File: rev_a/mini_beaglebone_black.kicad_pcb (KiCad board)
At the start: 2 copper layers, 4 parts

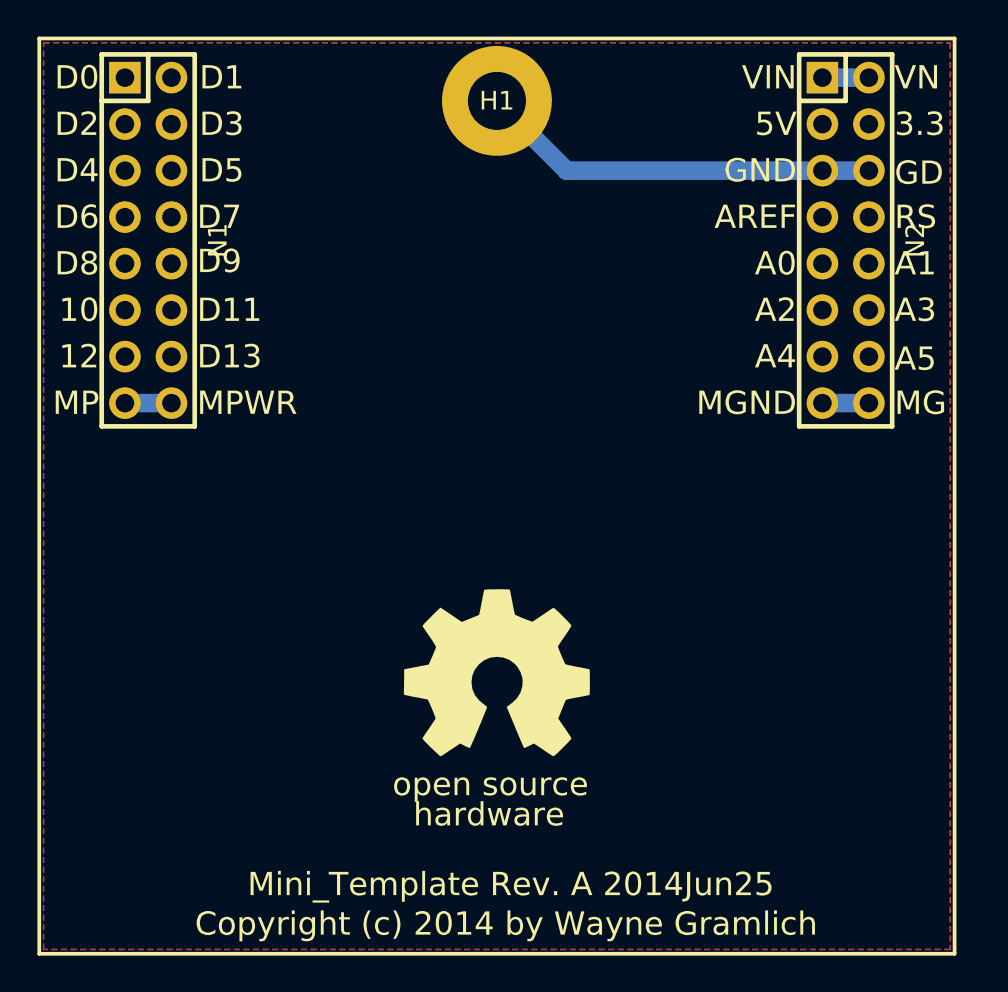
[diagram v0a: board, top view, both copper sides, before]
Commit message: Got first layout of BBB Mini-Shield done.
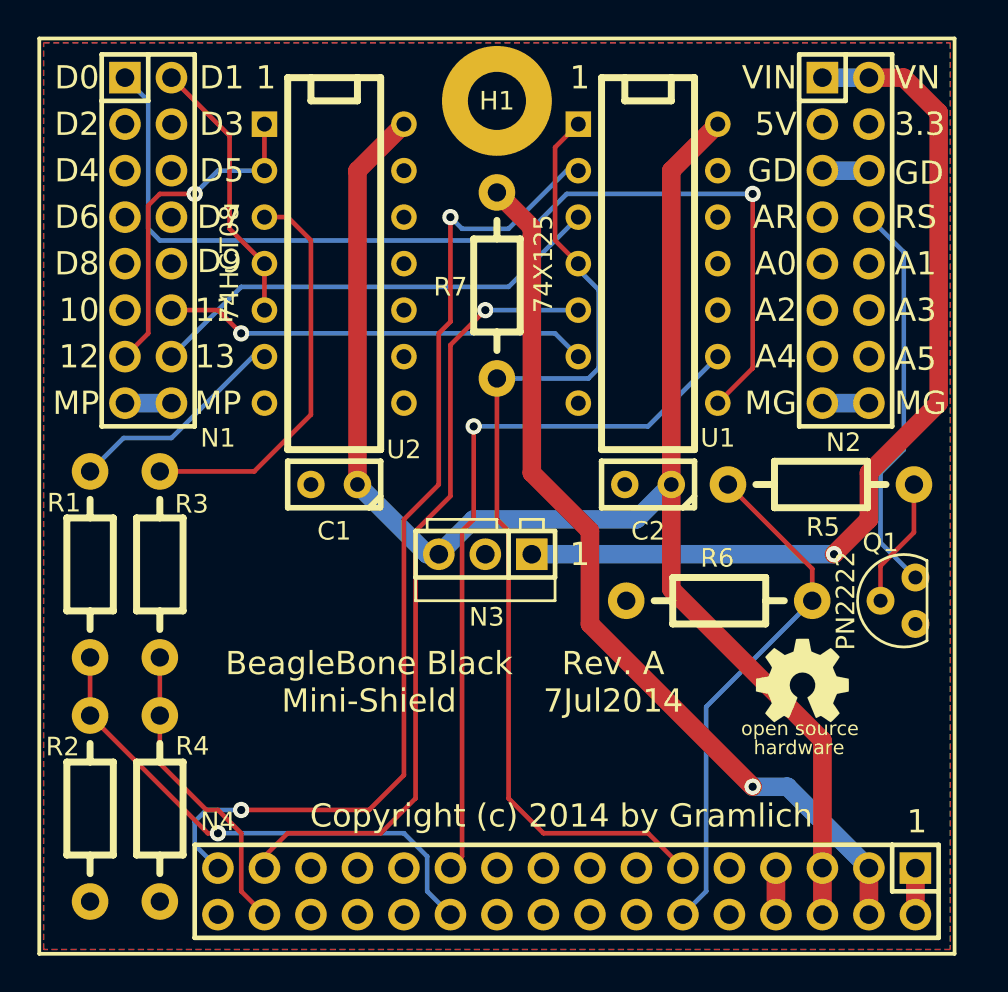
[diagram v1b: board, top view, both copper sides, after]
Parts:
- added C1: .1uF, Mini_BeagleBone_Black_Rev_A:Capacitor3MMDiscRM2.5, F.Cu at (92.7, 127.6)
- added C2: .1uF, Mini_BeagleBone_Black_Rev_A:Capacitor3MMDiscRM2.5, F.Cu at (109.9, 127.6)
- added N3: OKI-78SR-5/1.5-W36-C, Mini_BeagleBone_Black_Rev_A:OKI_DC_TO_DC_CONNECTOR, F.Cu at (101.0, 131.4)
- added N4: BBB_P9_HEADER, Mini_BeagleBone_Black_Rev_A:Pin_Header_Straight_2x16, F.Cu at (105.4, 149.9)
- added Q1: PN2222, Mini_BeagleBone_Black_Rev_A:TO92_123, F.Cu at (123.8, 134.0)
- added R1: 2K2 1%, Mini_BeagleBone_Black_Rev_A:Resistor_Horizontal_RM10mm, F.Cu at (79.4, 132.1)
- added R2: 3K3 1%, Mini_BeagleBone_Black_Rev_A:Resistor_Horizontal_RM10mm, F.Cu at (79.4, 145.4)
- added R3: 2K2 1%, Mini_BeagleBone_Black_Rev_A:Resistor_Horizontal_RM10mm, F.Cu at (83.2, 132.1)
- added R4: 3K3 1%, Mini_BeagleBone_Black_Rev_A:Resistor_Horizontal_RM10mm, F.Cu at (83.2, 145.4)
- added R5: 470, Mini_BeagleBone_Black_Rev_A:Resistor_Horizontal_RM10mm, F.Cu at (119.4, 127.6)
- added R6: 10K, Mini_BeagleBone_Black_Rev_A:Resistor_Horizontal_RM10mm, F.Cu at (113.7, 134.0)
- added R7: 10K, Mini_BeagleBone_Black_Rev_A:Resistor_Horizontal_RM10mm, F.Cu at (101.6, 116.8)
- added U1: 74X125, Mini_BeagleBone_Black_Rev_A:DIP-14__300, F.Cu at (109.9, 115.6)
- added U2: 74HCT08, Mini_BeagleBone_Black_Rev_A:DIP-14__300, F.Cu at (92.7, 115.6)
- G1: footprint Mini_BeagleBone_Black_Rev_A:OSHW_LOGO_400mil -> Mini_BeagleBone_Black_Rev_A:OSHW_LOGO_200mil
- moved G1 16.7 mm to (118.3, 138.3)
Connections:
- net /GND renamed GND
- N1 pad 1: (no net) -> /D0
- N1 pad 12: (no net) -> /D11
- N1 pad 13: (no net) -> /D12
- N1 pad 14: (no net) -> /D13
- N1 pad 2: (no net) -> /D1
- N2 pad 8: (no net) -> /~RESET
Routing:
- net VCC: track 0.00 -> 88.7 mm, vias 0 -> 1
- net Net-(N4-Pad11): track 0.00 -> 55.7 mm
- net Net-(N4-Pad31): track 0.00 -> 55.6 mm, vias 0 -> 2
- net /D0: track 0.00 -> 55.3 mm, vias 0 -> 1
- net /BB_VDD3V3: track 0.00 -> 49.1 mm, vias 0 -> 1
- net /VIN: track 2.54 -> 50.1 mm, vias 0 -> 1
- net Net-(N4-Pad29): track 0.00 -> 43.5 mm, vias 0 -> 1
- net Net-(N4-Pad21): track 0.00 -> 39.6 mm, vias 0 -> 1
- net Net-(N4-Pad22): track 0.00 -> 28.5 mm, vias 0 -> 1
- net Net-(N4-Pad12): track 0.00 -> 28.3 mm
- net /D13: track 0.00 -> 25.4 mm
- net /D11: track 0.00 -> 23.3 mm, vias 0 -> 1
- net /MISO_5V: track 0.00 -> 22.1 mm
- net /~RESET: track 0.00 -> 21.8 mm
- net /D12: track 0.00 -> 18.5 mm, vias 0 -> 1
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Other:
- board text added: "1"
- board text added: "11"
- board text added: "13"
- board text added: "AR"
- board text added: "BeagleBone Black Mini-Shield"
- board text added: "Copyright (c) 2014 by Gramlich"
- board text added: "Rev. A 6Jul2014"
- board text added: "Rev. A 7Jul2014"
- board text removed: "AREF"
- board text removed: "Copyright (c) 2014 by Wayne Gramlich"
- board text removed: "D11"
- board text removed: "D13"
- board text removed: "GND"
- board text removed: "MGND"
- board text removed: "MPWR"
- board text removed: "Mini_Template Rev. A 2014Jun25"

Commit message: Did another polishing sweep through the board.
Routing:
- net GND: track 5.08 -> 94.4 mm, vias 0 -> 4
- net /D0: track 55.3 -> 51.9 mm
- net /VIN: track 50.1 -> 48.7 mm
- net /D1: track 14.8 -> 15.9 mm
- net Net-(N4-Pad12): track 28.3 -> 28.6 mm, vias 0 -> 1
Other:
- board text added: "Rev. A 11Jul2014"
- board text added: "Rev. A1 11Jul2014"
- board text removed: "Rev. A 6Jul2014"
- board text removed: "Rev. A 7Jul2014"

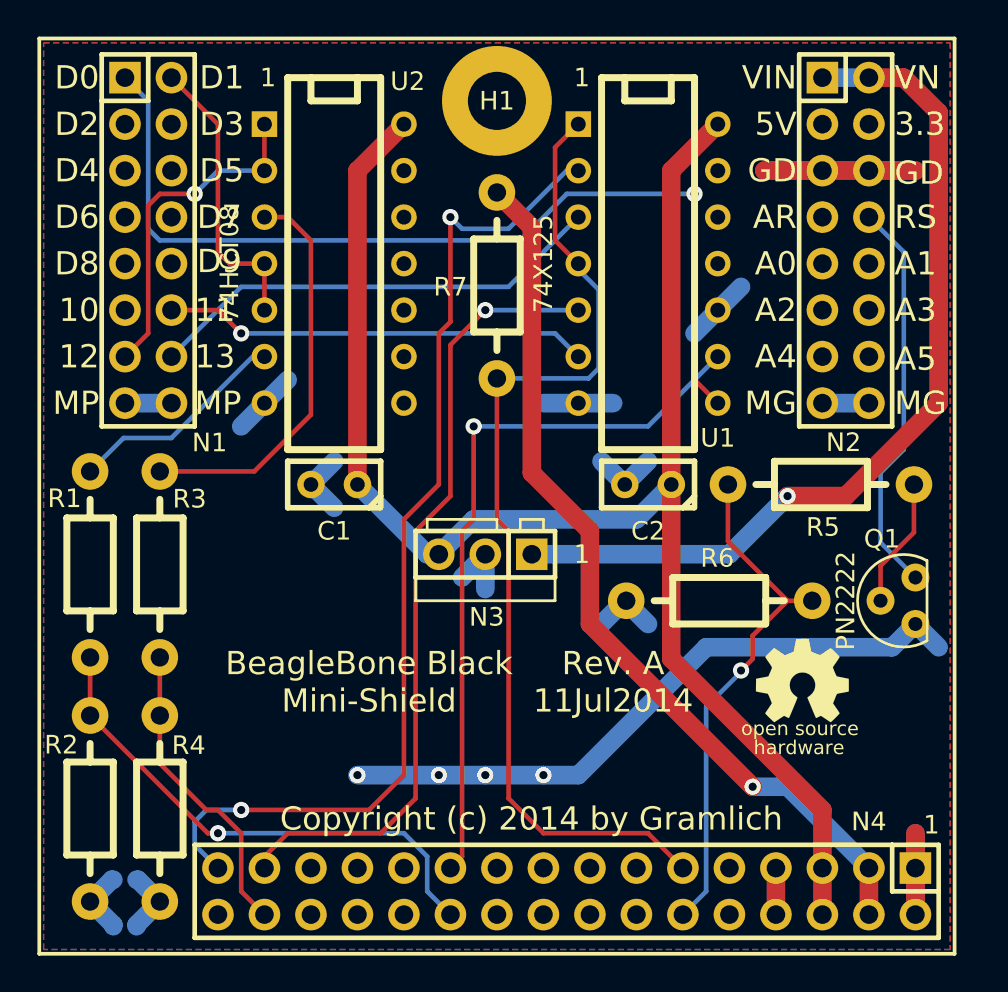
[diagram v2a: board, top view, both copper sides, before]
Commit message: Added Edge Cuts.
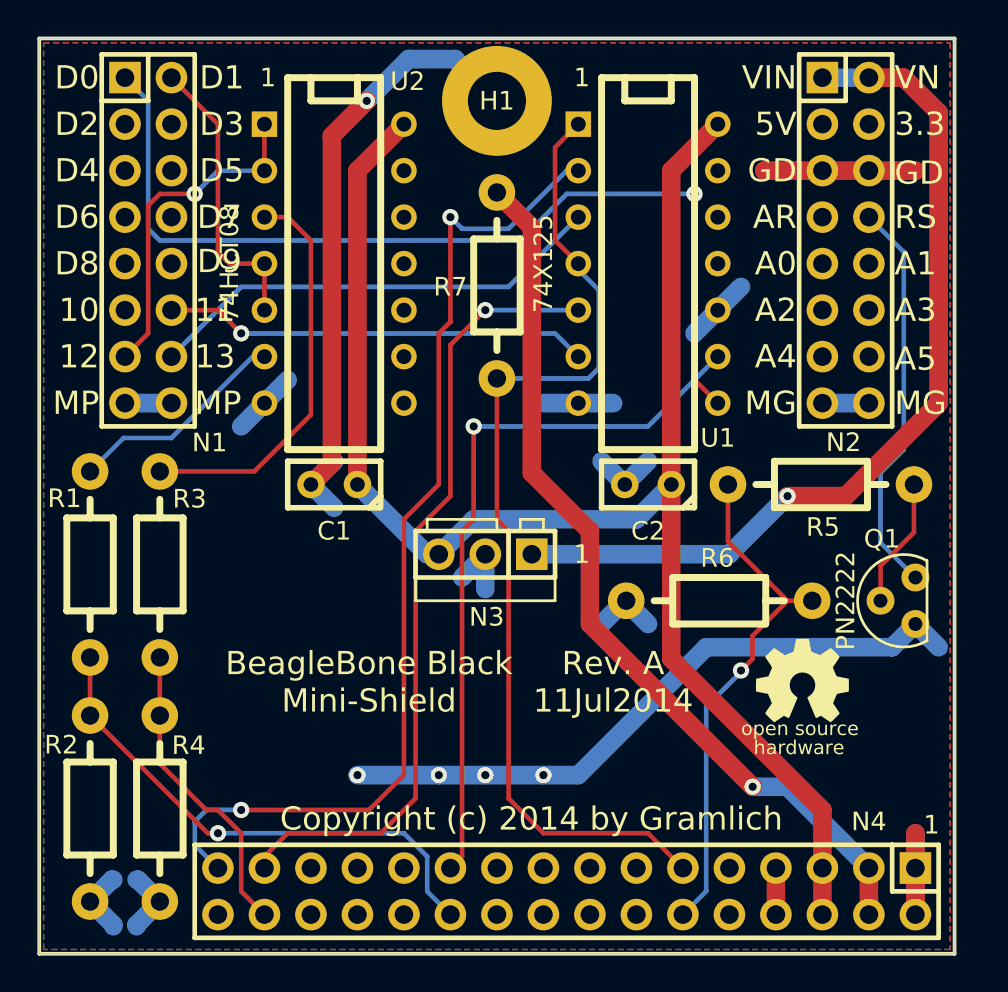
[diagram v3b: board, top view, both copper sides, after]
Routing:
- net GND: track 94.4 -> 125.6 mm, vias 4 -> 5
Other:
- board outline added: 50 x 50 mm

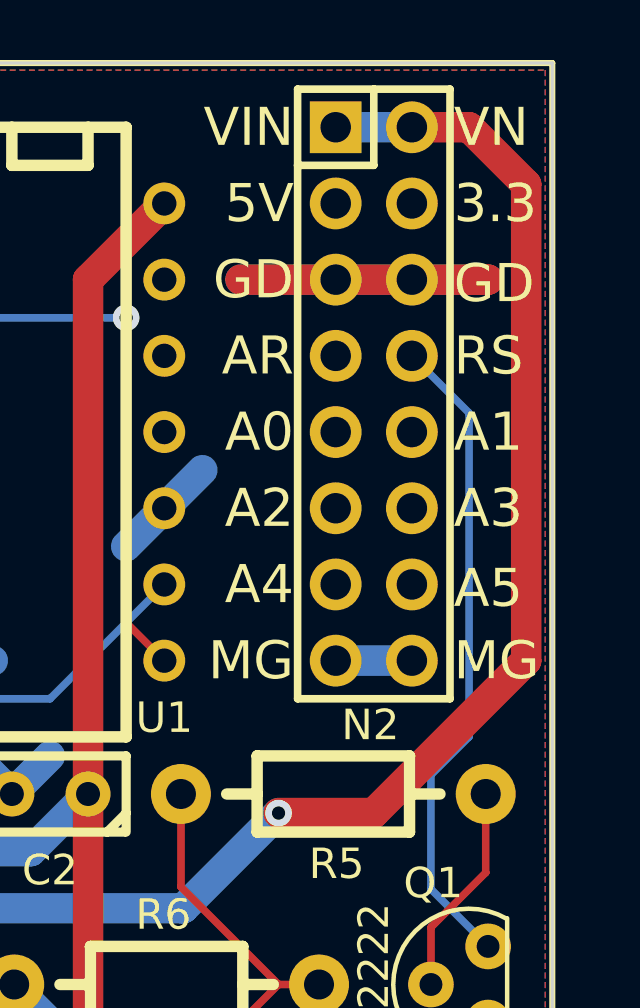
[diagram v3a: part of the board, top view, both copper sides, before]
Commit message: Moved one trace too close too PCB edge.
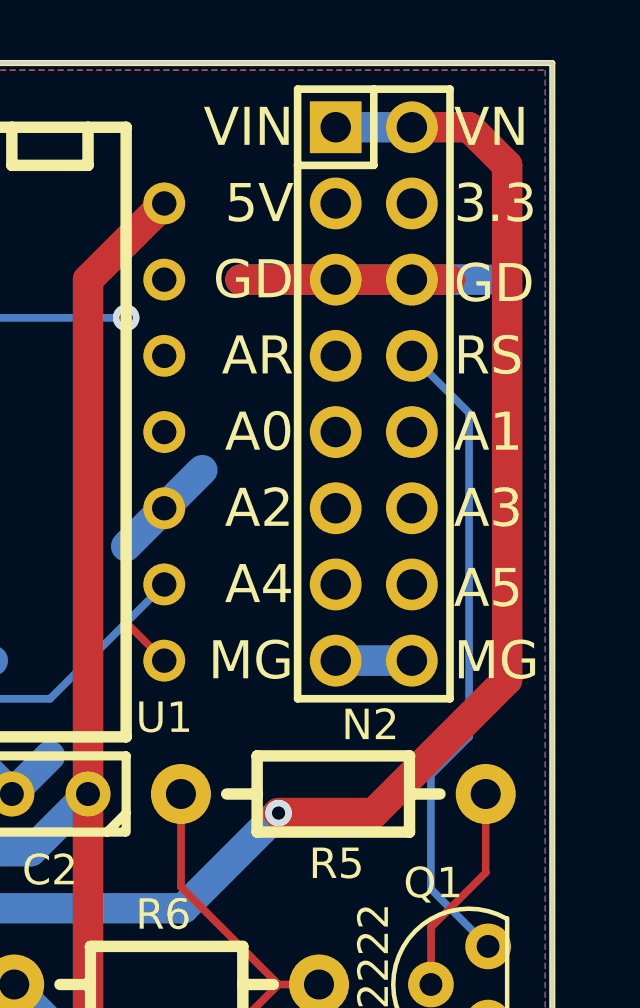
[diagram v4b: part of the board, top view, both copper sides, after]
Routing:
- net GND: track 125.6 -> 123.7 mm
- net /VIN: track 48.7 -> 48.1 mm
